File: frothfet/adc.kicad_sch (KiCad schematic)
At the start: 15 parts, among them U26 MCP3564R

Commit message: almost ready for routing.
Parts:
- removed R74: 10R, Resistor_SMD:R_0603_1608Metric, symbol Device:R_Small_US
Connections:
- no-connect marks 0 -> 1
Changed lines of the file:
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@@
 		(color 0 0 0 0)
 	)
+	(no_connect
+		(at 154.94 78.74)
+	)
 	(wire
 		(pts
@@
 	(wire
 		(pts
-			(xy 167.64 78.74) (xy 154.94 78.74)
-		)
-		(stroke
-			(width 0)
-			(type default)
-		)
-	)
-	(wire
-		(pts
 			(xy 187.96 88.9) (xy 187.96 106.68)
 		)
@@
 		(pts
 			(xy 135.89 53.34) (xy 135.89 54.61)
-		)
-		(stroke
-			(width 0)
-			(type default)
-		)
-	)
-	(wire
-		(pts
-			(xy 177.8 78.74) (xy 172.72 78.74)
 		)
 		(stroke
@@
 		(shape input)
 		(at 177.8 93.98 0)
-		(effects
-			(font
-				(size 1.27 1.27)
-			)
-			(justify left)
-		)
-	)
-	(hierarchical_label "MCLK"
-		(shape input)
-		(at 177.8 78.74 0)
 		(effects
 			(font
@@
 					(unit 1)
 				)
-			)
-		)
-	)
-	(symbol
-		(lib_id "Device:R_Small_US")
-		(at 170.18 78.74 90)
-		(unit 1)
-		(exclude_from_sim no)
-		(in_bom yes)
-		(on_board yes)
-		(dnp no)
-		(property "Reference" "R74"
-			(at 166.624 77.724 90)
-			(effects
-				(font
-					(size 1.27 1.27)
-				)
-			)
-		)
-		(property "Value" "10R"
-			(at 173.482 77.724 90)
-			(effects
-				(font
-					(size 1.27 1.27)
-				)
-			)
-		)
-		(property "Footprint" "Resistor_SMD:R_0603_1608Metric"
-			(at 170.18 78.74 0)
-			(effects
-				(font
-					(size 1.27 1.27)
-				)
-				(hide yes)
-			)
-		)
-		(property "Datasheet" "~"
-			(at 170.18 78.74 0)
-			(effects
-				(font
-					(size 1.27 1.27)
-				)
-				(hide yes)
-			)
-		)
-		(property "Description" ""
-			(at 170.18 78.74 0)
-			(effects
-				(font
-					(size 1.27 1.27)
-				)
-				(hide yes)
-			)
-		)
-		(property "LCSC" ""
-			(at 170.18 78.74 0)
-			(effects
-				(font
-					(size 1.27 1.27)
-				)
-				(hide yes)
-			)
-		)
-		(property "ALT" ""
-			(at 170.18 78.74 0)
-			(effects
-				(font
-					(size 1.27 1.27)
-				)
-				(hide yes)
-			)
-		)
-		(pin "1"
-		)
-		(pin "2"
-		)
-		(instances
-			(project "frothfet"
-				(path "/c83c6236-96e9-46ad-9d7a-9e2efa4a7966/6b72210f-69d1-4134-acd2-eb4247fc5d85"
-					(reference "R83")
-					(unit 1)
-				)
-				(path "/c83c6236-96e9-46ad-9d7a-9e2efa4a7966/b87f80e1-ecbd-4ee0-be26-4b252158928b"
-					(reference "R74")
-					(unit 1)
-				)

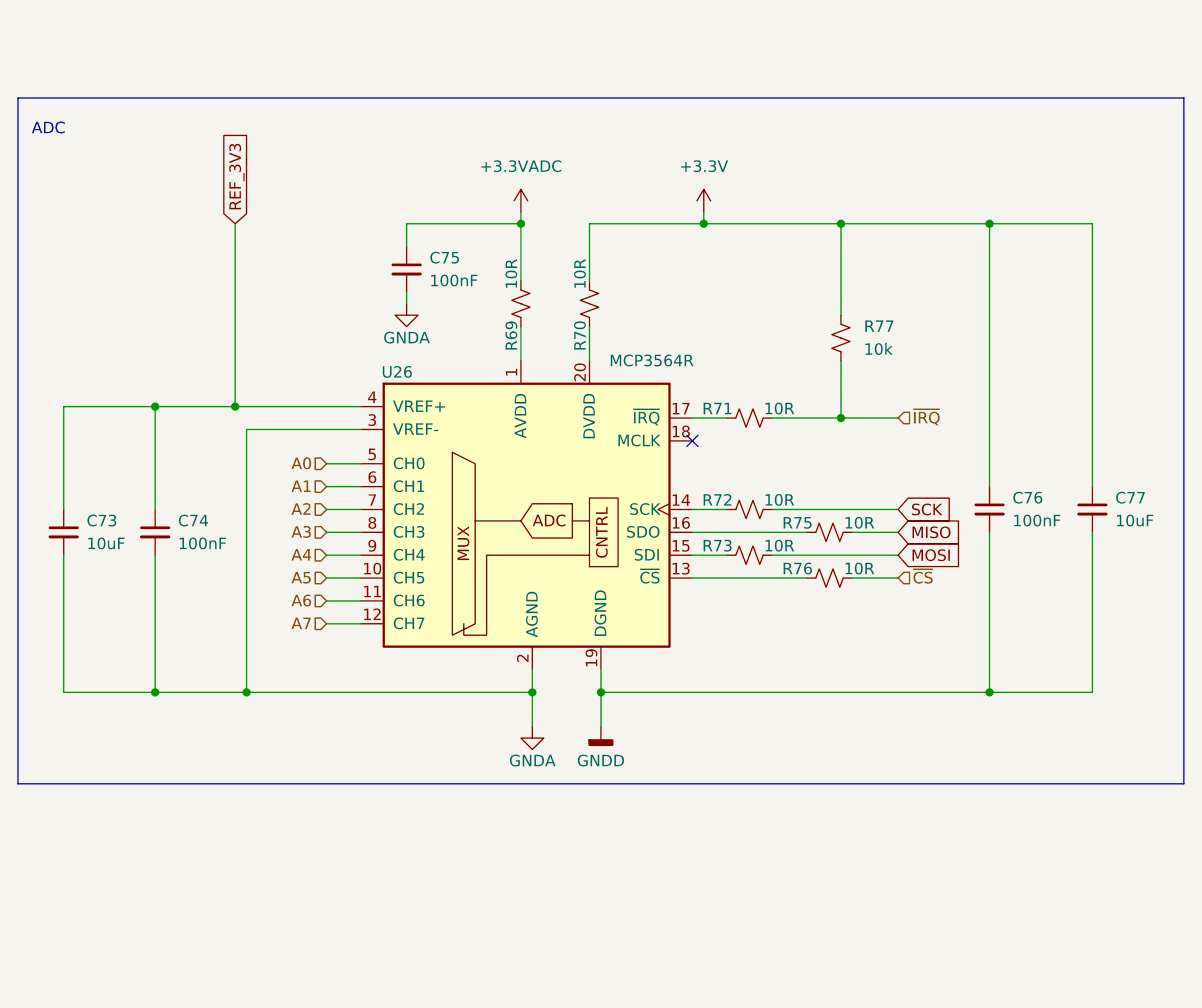
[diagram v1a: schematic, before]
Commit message: worked on the bom and footprint placement
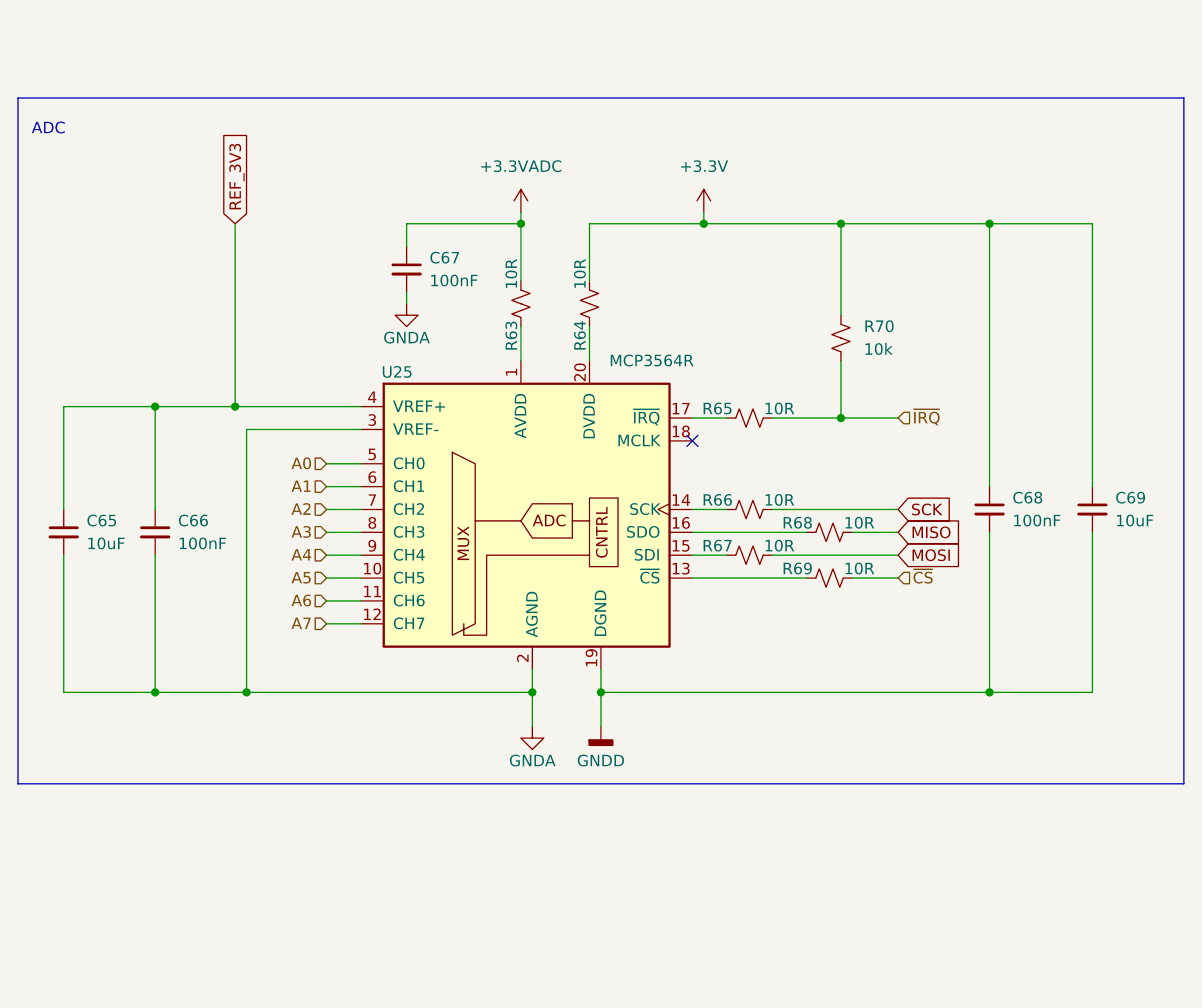
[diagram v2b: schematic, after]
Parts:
- C65: renamed from C73; LCSC C1952580 -> (none)
- C66: renamed from C74; LCSC C49678 -> (none)
- C67: renamed from C75; LCSC C49678 -> (none)
- C68: renamed from C76; LCSC C49678 -> (none)
- C69: renamed from C77; LCSC C49678 -> (none)
- renumbered R69 to R63, R70 to R64, R71 to R65, R72 to R66, R73 to R67, R75 to R68, R76 to R69, R77 to R70, U26 to U25

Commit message: changed the adc voltage regulator and vref to more common parts.
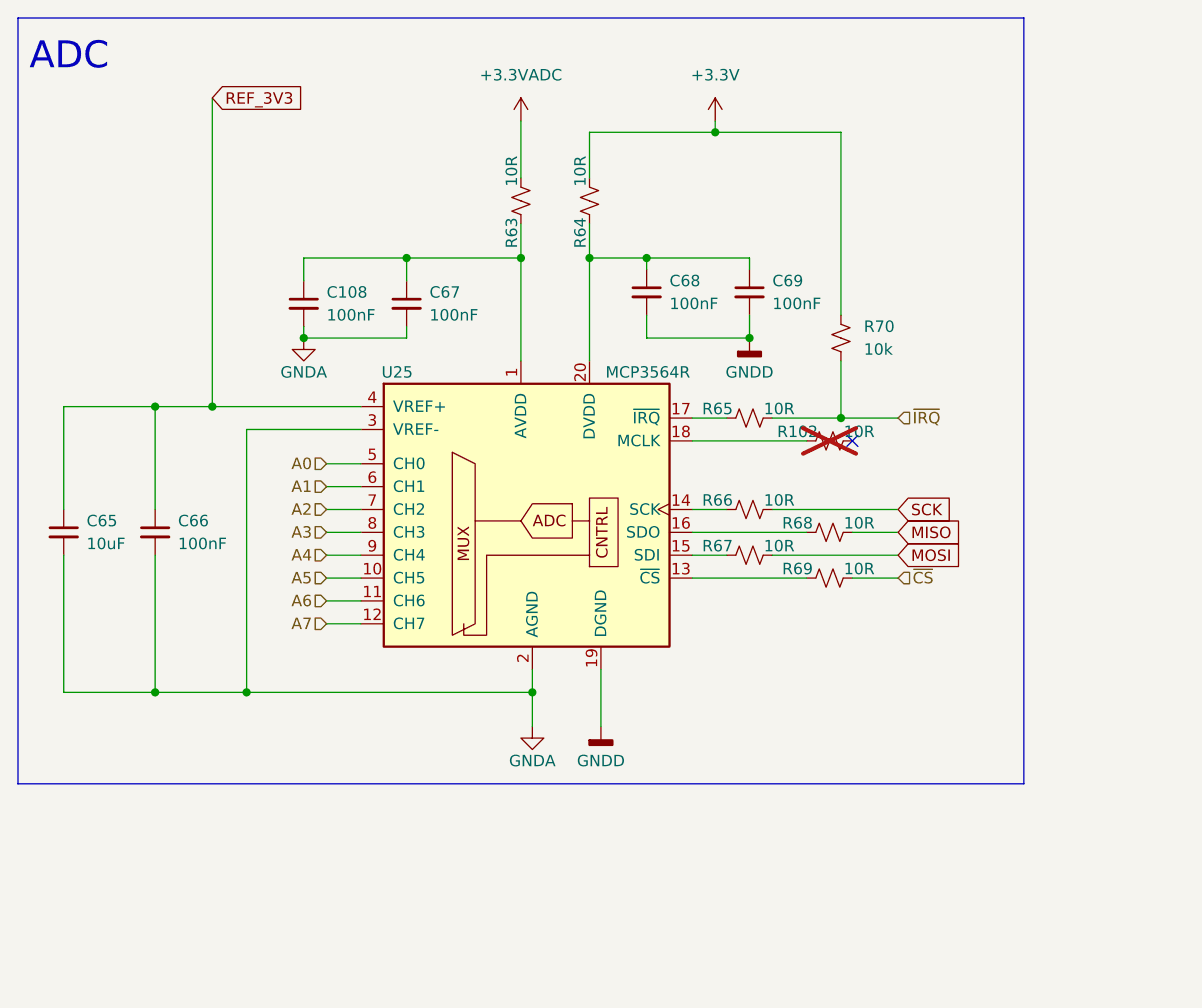
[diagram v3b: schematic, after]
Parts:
- added C108: 100nF, Capacitor_SMD:C_0603_1608Metric, symbol Device:C_Small
- added R102: 10R, Resistor_SMD:R_0603_1608Metric, symbol Device:R_Small_US
- C69: value 10uF -> 100nF
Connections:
- net +3.3V: no longer C68.1, C69.1
- net +3.3VADC: no longer C67.1
- net GNDA: now also C108.2
- net at R63.1, U25.1 (AVDD): now also C67.1, C108.1
- net at R64.1, U25.20 (DVDD): now also C68.1, C69.1
- net at U25.18 (MCLK): now also R102.1
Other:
- moved on the sheet: C67, C68, C69, R63, R64

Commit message: lots of work on the analog system
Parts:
- added FB3: BLM31PG601SN1L, Inductor_SMD:L_1206_3216Metric, symbol Device:FerriteBead_Small
- renumbered C108 to C67, C67 to C68, C68 to C69, C69 to C70, R102 to R68, R68 to R69, R69 to R70, R70 to R71
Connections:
- net GNDA: now also FB3.1
- net GNDD: now also FB3.2
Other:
- moved on the sheet: C65, C66, C67, C68, C69, C70, R63, R64, R65, R66, R67, R68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

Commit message: moved back to a single ground plane
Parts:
- FB3: now not fitted
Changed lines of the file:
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@@
 		(in_bom yes)
 		(on_board yes)
-		(dnp no)
+		(dnp yes)
 		(fields_autoplaced yes)
 		(property "Reference" "FB3"

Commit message: imported latest esp32-s3 module
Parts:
- renumbered FB3 to FB1
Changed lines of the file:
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@@
 		(dnp no)
 		(fields_autoplaced yes)
-		(property "Reference" "#PWR094"
+		(property "Reference" "#PWR096"
 			(at 163.83 67.31 0)
 			(effects
@@
 			(project "frothfet"
 				(path "/c83c6236-96e9-46ad-9d7a-9e2efa4a7966/6b72210f-69d1-4134-acd2-eb4247fc5d85"
-					(reference "#PWR099")
-					(unit 1)
-				)
-				(path "/c83c6236-96e9-46ad-9d7a-9e2efa4a7966/b87f80e1-ecbd-4ee0-be26-4b252158928b"
-					(reference "#PWR094")
+					(reference "#PWR0102")
+					(unit 1)
+				)
+				(path "/c83c6236-96e9-46ad-9d7a-9e2efa4a7966/b87f80e1-ecbd-4ee0-be26-4b252158928b"
+					(reference "#PWR096")
 					(unit 1)
 				)
@@
 		(dnp no)
 		(fields_autoplaced yes)
-		(property "Reference" "#PWR093"
+		(property "Reference" "#PWR095"
 			(at 151.13 139.7 0)
 			(effects
@@
 			(project "frothfet"
 				(path "/c83c6236-96e9-46ad-9d7a-9e2efa4a7966/6b72210f-69d1-4134-acd2-eb4247fc5d85"
-					(reference "#PWR098")
-					(unit 1)
-				)
-				(path "/c83c6236-96e9-46ad-9d7a-9e2efa4a7966/b87f80e1-ecbd-4ee0-be26-4b252158928b"
-					(reference "#PWR093")
+					(reference "#PWR0101")
+					(unit 1)
+				)
+				(path "/c83c6236-96e9-46ad-9d7a-9e2efa4a7966/b87f80e1-ecbd-4ee0-be26-4b252158928b"
+					(reference "#PWR095")
 					(unit 1)
 				)
@@
 		(on_board yes)
 		(dnp no)
-		(property "Reference" "#PWR0117"
+		(property "Reference" "#PWR094"
 			(at 143.51 139.7 0)
 			(effects
@@
 			(project ""
 				(path "/c83c6236-96e9-46ad-9d7a-9e2efa4a7966/6b72210f-69d1-4134-acd2-eb4247fc5d85"
-					(reference "#PWR0118")
-					(unit 1)
-				)
-				(path "/c83c6236-96e9-46ad-9d7a-9e2efa4a7966/b87f80e1-ecbd-4ee0-be26-4b252158928b"
-					(reference "#PWR0117")
+					(reference "#PWR0100")
+					(unit 1)
+				)
+				(path "/c83c6236-96e9-46ad-9d7a-9e2efa4a7966/b87f80e1-ecbd-4ee0-be26-4b252158928b"
+					(reference "#PWR094")
 					(unit 1)
 				)
@@
 		(dnp no)
 		(fields_autoplaced yes)
-		(property "Reference" "#PWR092"
+		(property "Reference" "#PWR093"
 			(at 146.05 64.77 0)
 			(effects
@@
 			(project "frothfet"
 				(path "/c83c6236-96e9-46ad-9d7a-9e2efa4a7966/6b72210f-69d1-4134-acd2-eb4247fc5d85"
-					(reference "#PWR097")
-					(unit 1)
-				)
-				(path "/c83c6236-96e9-46ad-9d7a-9e2efa4a7966/b87f80e1-ecbd-4ee0-be26-4b252158928b"
-					(reference "#PWR092")
+					(reference "#PWR099")
+					(unit 1)
+				)
+				(path "/c83c6236-96e9-46ad-9d7a-9e2efa4a7966/b87f80e1-ecbd-4ee0-be26-4b252158928b"
+					(reference "#PWR093")
 					(unit 1)
 				)
@@
 		(on_board yes)
 		(dnp no)
-		(property "Reference" "#PWR091"
+		(property "Reference" "#PWR092"
 			(at 118.11 93.98 0)
 			(effects
@@
 			(project "frothfet"
 				(path "/c83c6236-96e9-46ad-9d7a-9e2efa4a7966/6b72210f-69d1-4134-acd2-eb4247fc5d85"
-					(reference "#PWR096")
-					(unit 1)
-				)
-				(path "/c83c6236-96e9-46ad-9d7a-9e2efa4a7966/b87f80e1-ecbd-4ee0-be26-4b252158928b"
-					(reference "#PWR091")
+					(reference "#PWR098")
+					(unit 1)
+				)
+				(path "/c83c6236-96e9-46ad-9d7a-9e2efa4a7966/b87f80e1-ecbd-4ee0-be26-4b252158928b"
+					(reference "#PWR092")
 					(unit 1)
 				)
@@
 		(dnp yes)
 		(fields_autoplaced yes)
-		(property "Reference" "FB3"
+		(property "Reference" "FB1"
 			(at 147.2819 124.46 90)
 			(effects
@@
 			(project ""
 				(path "/c83c6236-96e9-46ad-9d7a-9e2efa4a7966/6b72210f-69d1-4134-acd2-eb4247fc5d85"
-					(reference "FB4")
-					(unit 1)
-				)
-				(path "/c83c6236-96e9-46ad-9d7a-9e2efa4a7966/b87f80e1-ecbd-4ee0-be26-4b252158928b"
-					(reference "FB3")
+					(reference "FB2")
+					(unit 1)
+				)
+				(path "/c83c6236-96e9-46ad-9d7a-9e2efa4a7966/b87f80e1-ecbd-4ee0-be26-4b252158928b"
+					(reference "FB1")
 					(unit 1)
 				)
@@
 		(dnp no)
 		(fields_autoplaced yes)
-		(property "Reference" "#PWR095"
+		(property "Reference" "#PWR097"
 			(at 167.64 93.98 0)
 			(effects
@@
 			(project "frothfet"
 				(path "/c83c6236-96e9-46ad-9d7a-9e2efa4a7966/6b72210f-69d1-4134-acd2-eb4247fc5d85"
-					(reference "#PWR0100")
-					(unit 1)
-				)
-				(path "/c83c6236-96e9-46ad-9d7a-9e2efa4a7966/b87f80e1-ecbd-4ee0-be26-4b252158928b"
-					(reference "#PWR095")
-					(unit 1)
-				)
+					(reference "#PWR0103")
+					(unit 1)
+				)
+				(path "/c83c6236-96e9-46ad-9d7a-9e2efa4a7966/b87f80e1-ecbd-4ee0-be26-4b252158928b"
+					(reference "#PWR097")
+					(unit 1)
+				)

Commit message: silkscreen done, erc+drc passing
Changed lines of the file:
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@@
+	)
+	(symbol
+		(lib_id "power:PWR_FLAG")
+		(at 129.54 78.74 0)
+		(unit 1)
+		(exclude_from_sim no)
+		(in_bom yes)
+		(on_board yes)
+		(dnp no)
+		(fields_autoplaced yes)
+		(property "Reference" "#FLG013"
+			(at 129.54 76.835 0)
+			(effects
+				(font
+					(size 1.27 1.27)
+				)
+				(hide yes)
+			)
+		)
+		(property "Value" "PWR_FLAG"
+			(at 129.54 73.66 0)
+			(effects
+				(font
+					(size 1.27 1.27)
+				)
+			)
+		)
+		(property "Footprint" ""
+			(at 129.54 78.74 0)
+			(effects
+				(font
+					(size 1.27 1.27)
+				)
+				(hide yes)
+			)
+		)
+		(property "Datasheet" "~"
+			(at 129.54 78.74 0)
+			(effects
+				(font
+					(size 1.27 1.27)
+				)
+				(hide yes)
+			)
+		)
+		(property "Description" "Special symbol for telling ERC where power comes from"
+			(at 129.54 78.74 0)
+			(effects
+				(font
+					(size 1.27 1.27)
+				)
+				(hide yes)
+			)
+		)
+		(pin "1"
+		)
+		(instances
+			(project ""
+				(path "/c83c6236-96e9-46ad-9d7a-9e2efa4a7966/6b72210f-69d1-4134-acd2-eb4247fc5d85"
+					(reference "#FLG014")
+					(unit 1)
+				)
+				(path "/c83c6236-96e9-46ad-9d7a-9e2efa4a7966/b87f80e1-ecbd-4ee0-be26-4b252158928b"
+					(reference "#FLG013")
+					(unit 1)
+				)
+			)
+		)
 	)
 	(symbol
@@
 					(unit 1)
 				)
+			)
+		)
+	)
+	(symbol
+		(lib_id "power:PWR_FLAG")
+		(at 156.21 78.74 0)
+		(unit 1)
+		(exclude_from_sim no)
+		(in_bom yes)
+		(on_board yes)
+		(dnp no)
+		(fields_autoplaced yes)
+		(property "Reference" "#FLG015"
+			(at 156.21 76.835 0)
+			(effects
+				(font
+					(size 1.27 1.27)
+				)
+				(hide yes)
+			)
+		)
+		(property "Value" "PWR_FLAG"
+			(at 156.21 73.66 0)
+			(effects
+				(font
+					(size 1.27 1.27)
+				)
+			)
+		)
+		(property "Footprint" ""
+			(at 156.21 78.74 0)
+			(effects
+				(font
+					(size 1.27 1.27)
+				)
+				(hide yes)
+			)
+		)
+		(property "Datasheet" "~"
+			(at 156.21 78.74 0)
+			(effects
+				(font
+					(size 1.27 1.27)
+				)
+				(hide yes)
+			)
+		)
+		(property "Description" "Special symbol for telling ERC where power comes from"
+			(at 156.21 78.74 0)
+			(effects
+				(font
+					(size 1.27 1.27)
+				)
+				(hide yes)
+			)
+		)
+		(pin "1"
+		)
+		(instances
+			(project "frothfet"
+				(path "/c83c6236-96e9-46ad-9d7a-9e2efa4a7966/6b72210f-69d1-4134-acd2-eb4247fc5d85"
+					(reference "#FLG016")
+					(unit 1)
+				)
+				(path "/c83c6236-96e9-46ad-9d7a-9e2efa4a7966/b87f80e1-ecbd-4ee0-be26-4b252158928b"
+					(reference "#FLG015")
+					(unit 1)
+				)

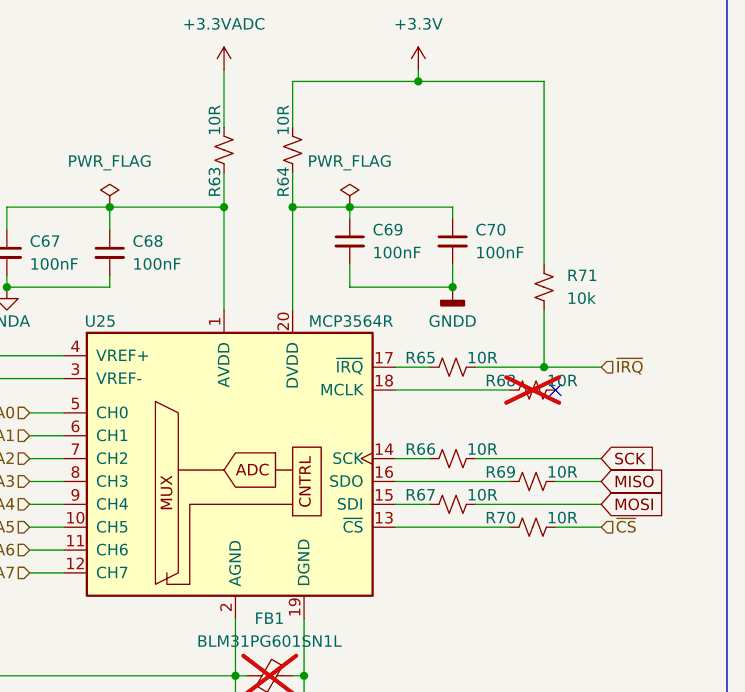
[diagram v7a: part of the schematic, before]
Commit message: pulled in updated esp32-s3 schematic
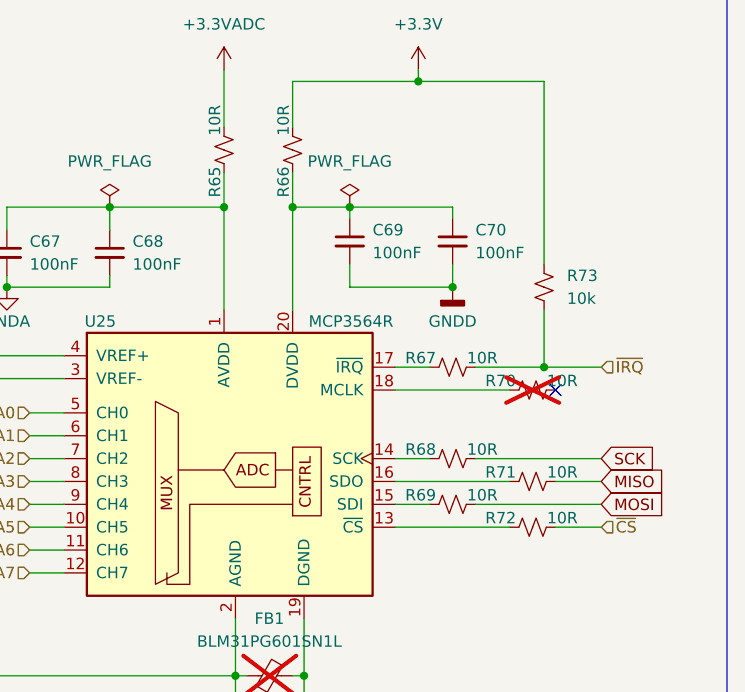
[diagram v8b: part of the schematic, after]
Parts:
- renumbered R63 to R65, R64 to R66, R65 to R67, R66 to R68, R67 to R69, R68 to R70, R69 to R71, R70 to R72, R71 to R73
